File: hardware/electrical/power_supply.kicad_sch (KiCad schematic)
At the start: 0 parts

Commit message: initial commit of power module schematic and PCB
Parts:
- added C1: 4.7uF, Capacitor_SMD:C_0402_1005Metric, symbol Device:C
- added C2: 0.1uF, Capacitor_SMD:C_0402_1005Metric, symbol Device:C
- added C3: 10uF, Capacitor_SMD:C_0402_1005Metric, symbol Device:C
- added C4, C5: 1uF, Capacitor_SMD:C_0402_1005Metric, symbol Device:C
- added D1: LED, LED_SMD:LED_1206_3216Metric, symbol Device:LED
- added D2: D_Schottky, Diode_THT:D_DO-41_SOD81_P2.54mm_Vertical_AnodeUp, symbol Device:D_Schottky
- added J1: USB_OTG, Connector_USB:USB_Micro-B_GCT_USB3076-30-A, symbol Connector:USB_OTG
- added J2: Conn_01x02_Female, Connector_PinSocket_2.00mm:PinSocket_1x02_P2.00mm_Vertical, symbol Connector:Conn_01x02_Female
- added J3: Conn_01x02_Male, Connector_PinHeader_2.00mm:PinHeader_1x02_P2.00mm_Vertical, symbol Connector:Conn_01x02_Male
- added Q1, Q2: IRLZ34N, Package_TO_SOT_SMD:SOT-23, symbol Transistor_FET:IRLZ34N
- added Q3, Q4: IRLML5203, Package_TO_SOT_SMD:SOT-23, symbol Transistor_FET:IRLML5203
- added R1: R, Resistor_SMD:R_0805_2012Metric_Pad1.20x1.40mm_HandSolder, symbol Device:R
- added R2: 470, Resistor_SMD:R_0805_2012Metric_Pad1.20x1.40mm_HandSolder, symbol Device:R
- added R3: 2.7k, Resistor_SMD:R_0805_2012Metric_Pad1.20x1.40mm_HandSolder, symbol Device:R
- added R4: 100, Resistor_SMD:R_0805_2012Metric_Pad1.20x1.40mm_HandSolder, symbol Device:R
- added R5, R6: 1k, Resistor_SMD:R_0805_2012Metric_Pad1.20x1.40mm_HandSolder, symbol Device:R
- added SW1: SW_DIP_x01, Connector_PinHeader_2.00mm:PinHeader_1x02_P2.00mm_Vertical, symbol Switch:SW_DIP_x01
- added U1: MCP73831-2-OT, Package_TO_SOT_SMD:SOT-23-5, symbol Battery_Management:MCP73831-2-OT
- added U2: AP9101CK6, Package_TO_SOT_SMD:SOT-23-6, symbol Battery_Management:AP9101CK6
- added U3: MCP1700-3302E_SOT23, Package_TO_SOT_SMD:SOT-23, symbol Regulator_Linear:MCP1700-3302E_SOT23
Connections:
- new net: Q2.1 (G), U2.1 (DO)
- new net: Q1.2 (D), Q2.2 (D)
- new net: Q3.1 (G), Q4.1 (G), R6.1
- new net: C3.2, D2.1 (K), Q4.3 (D), SW1.1
- new net: Q3.2 (S), Q4.2 (S)
- new net: R1.2, U1.5 (PROG)
- new net: Q1.1 (G), U2.3 (CO)
- new net: R2.2, U1.1 (STAT)
- new net: R3.1, U2.2 (VM)
- new net: C2.2, R4.1, U2.5 (VDD)
- new net: D1.1 (K), R2.1
- new net +3V3: C5.2, J2.1 (Pin_1), U3.2 (VO)
- new net +5V: D1.2 (A), D2.2 (A), J1.1 (VBUS), R5.2, R6.2, U1.4 (VDD)
- new net GND: C1.1, C3.1, C4.1, C5.1, J1.5 (GND), J2.2 (Pin_2), Q1.3 (S), R1.1, R3.2, U1.2 (VSS), U3.1 (GND)
- new net LIPO+: C1.2, J3.1 (Pin_1), Q3.3 (D), R4.2, U1.3 (VBAT)
- new net LIPO-: C2.1, J3.2 (Pin_2), Q2.3 (S), R5.1, U2.6 (VSS)
- new net OUT+: C4.2, SW1.2, U3.3 (VI)
- no-connect marks 0 -> 4
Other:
- note added: "Battery Protection Circuit"
- note added: "Charge indicator"
- note added: "To LiPo"
- note added: "To Micro USB Charger"
- note added: "To Voltage Regulator"
- note added: "Voltage Regulators (LDO)"

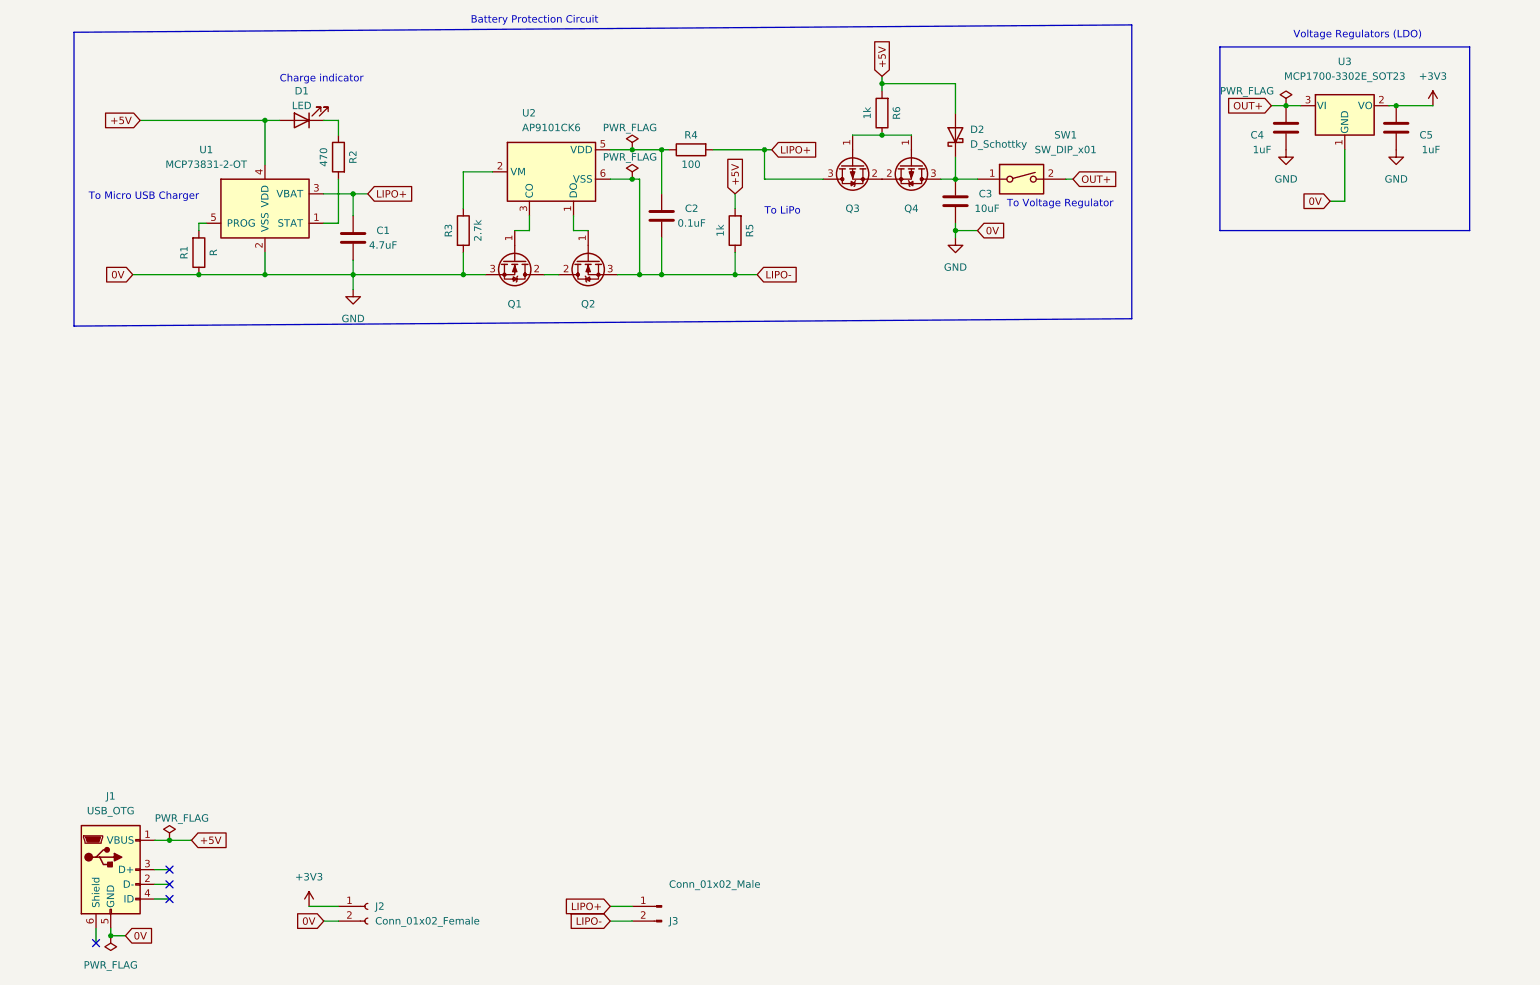
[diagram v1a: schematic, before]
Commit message: Power schematic style changes * Use power ports over global labels where possible * Replace 3.3V connector with test points * Make all component labels upright
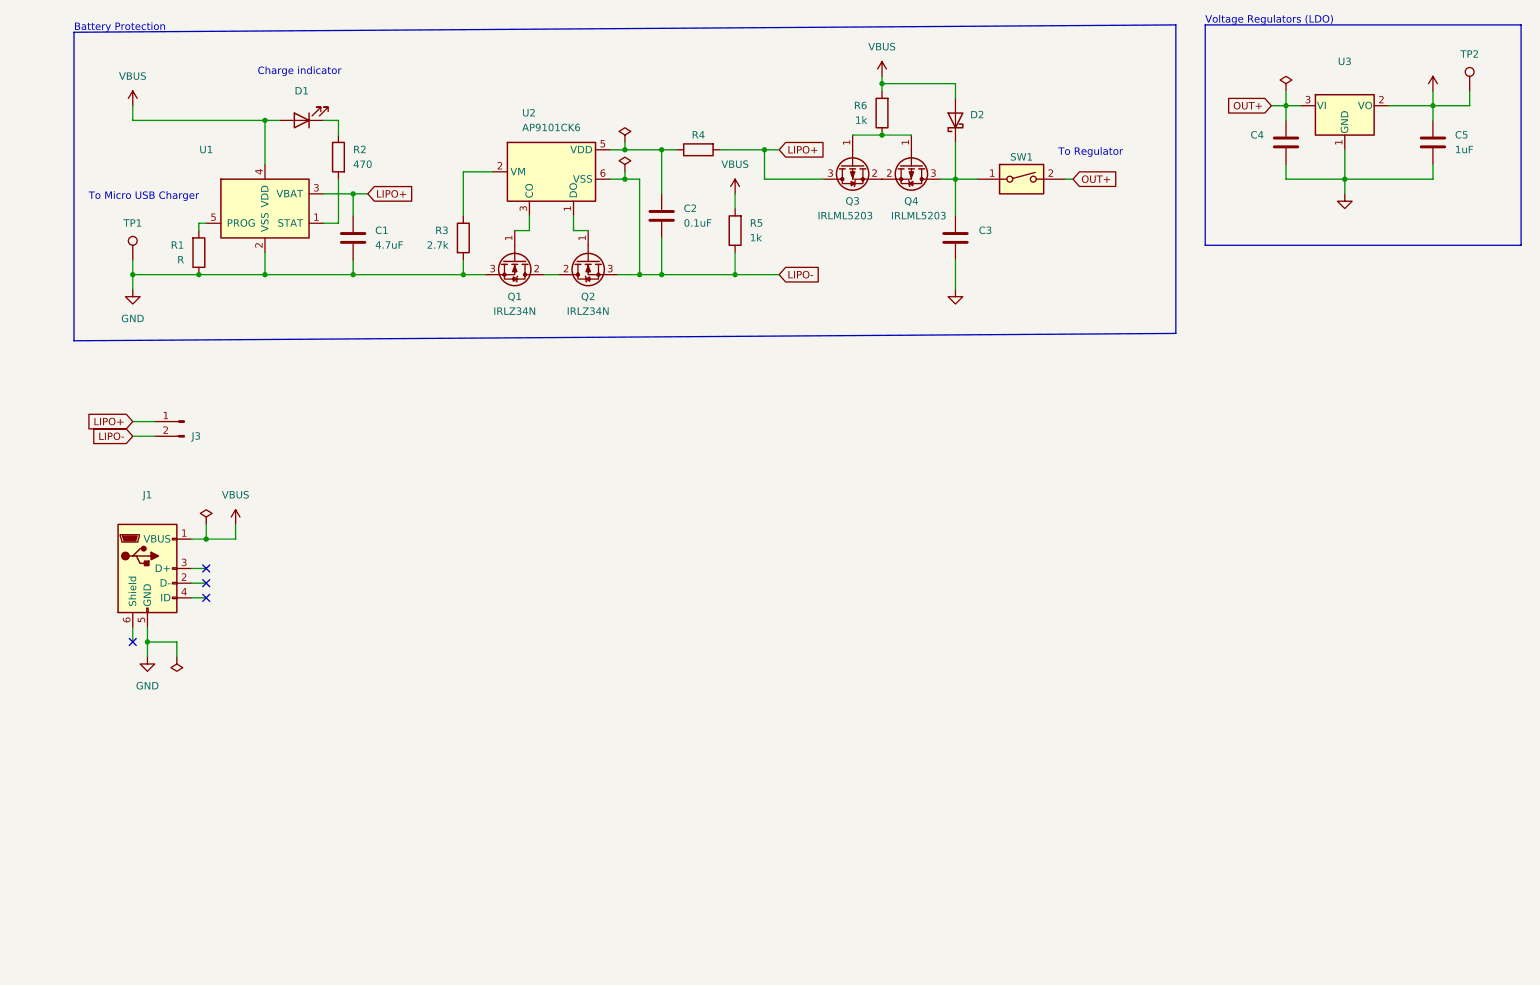
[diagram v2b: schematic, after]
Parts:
- removed J2: Conn_01x02_Female, Connector_PinSocket_2.00mm:PinSocket_1x02_P2.00mm_Vertical, symbol Connector:Conn_01x02_Female
- added TP1, TP2: TestPoint, symbol Connector:TestPoint
- C1, C2, C5: footprint Capacitor_SMD:C_0402_1005Metric -> (none)
- C3: value 10uF -> (none); footprint Capacitor_SMD:C_0402_1005Metric -> (none)
- C4: value 1uF -> (none); footprint Capacitor_SMD:C_0402_1005Metric -> (none)
- D1: value LED -> (none); footprint LED_SMD:LED_1206_3216Metric -> (none)
- D2: value D_Schottky -> (none); footprint Diode_THT:D_DO-41_SOD81_P2.54mm_Vertical_AnodeUp -> (none)
- J1: value USB_OTG -> (none); footprint Connector_USB:USB_Micro-B_GCT_USB3076-30-A -> (none)
- J3: value Conn_01x02_Male -> (none); footprint Connector_PinHeader_2.00mm:PinHeader_1x02_P2.00mm_Vertical -> (none)
- Q1, Q2, Q3, Q4: footprint Package_TO_SOT_SMD:SOT-23 -> (none)
- R1, R2, R3, R5, R6: footprint Resistor_SMD:R_0805_2012Metric_Pad1.20x1.40mm_HandSolder -> (none)
- R4: value 100 -> (none); footprint Resistor_SMD:R_0805_2012Metric_Pad1.20x1.40mm_HandSolder -> (none)
- SW1: value SW_DIP_x01 -> (none); footprint Connector_PinHeader_2.00mm:PinHeader_1x02_P2.00mm_Vertical -> (none)
- U1: value MCP73831-2-OT -> (none); footprint Package_TO_SOT_SMD:SOT-23-5 -> (none)
- U3: value MCP1700-3302E_SOT23 -> (none); footprint Package_TO_SOT_SMD:SOT-23 -> (none)
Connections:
- net +3V3: now also TP2.1
- net GND: now also TP1.1
- net +5V renamed VBUS
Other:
- note added: "Battery Protection"
- note added: "To Regulator"
- note removed: "Battery Protection Circuit"
- note removed: "To LiPo"
- note removed: "To Voltage Regulator"
- moved on the sheet: C3, C4, C5, D2, J1, J3, R3, R4

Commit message: grouped test points
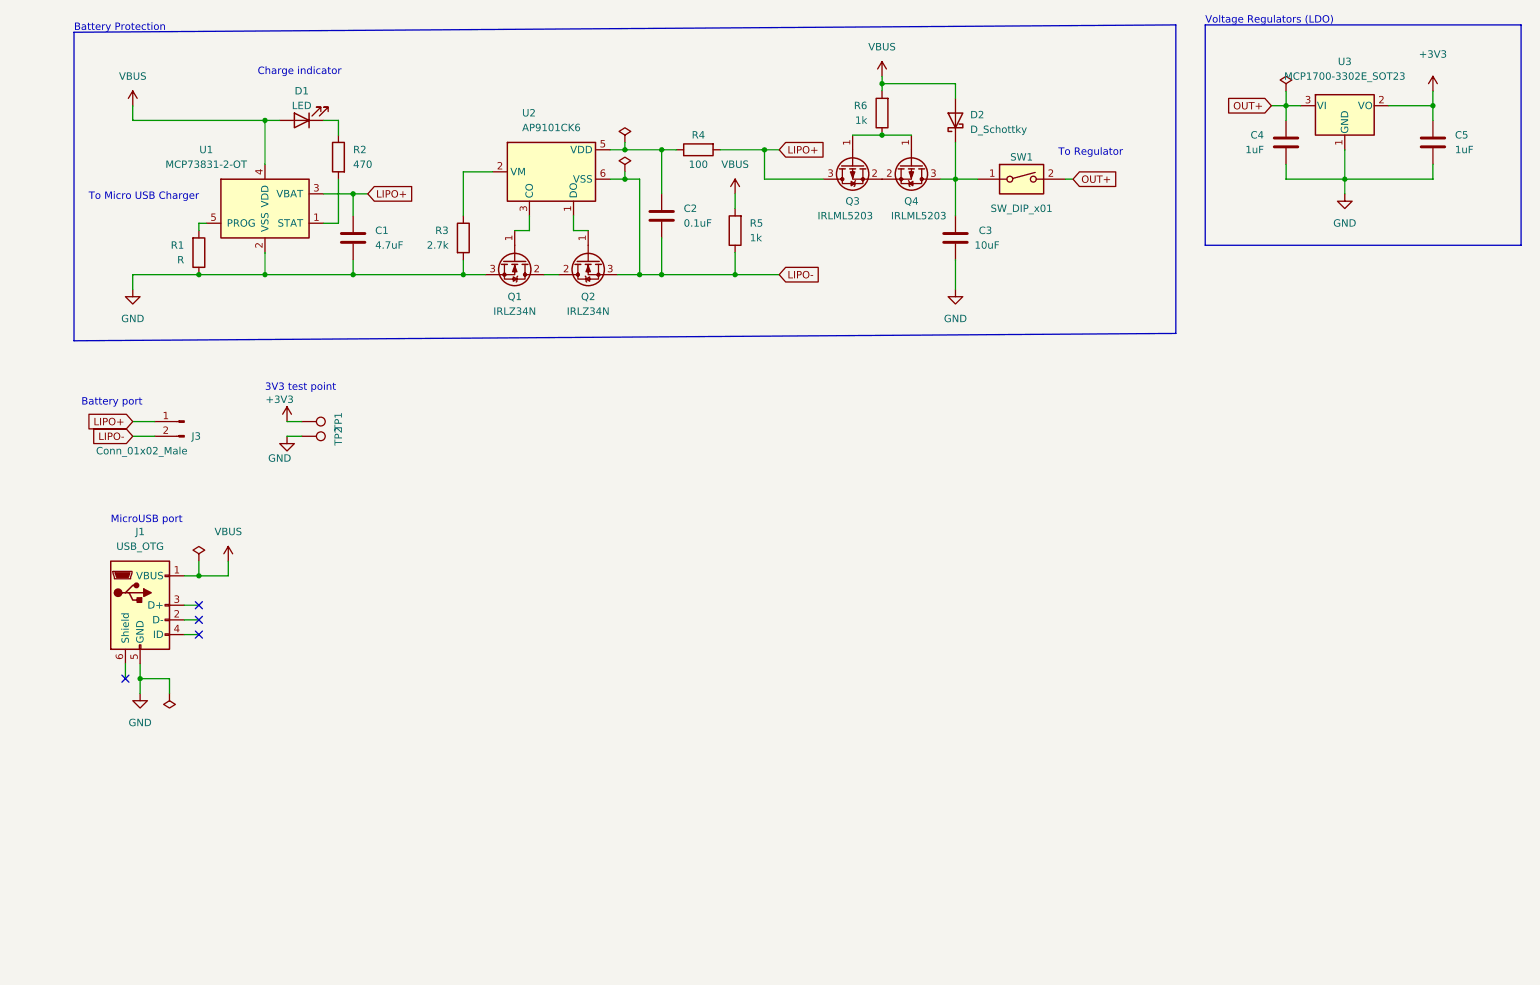
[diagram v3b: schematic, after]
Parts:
- C1, C2, C5: footprint (none) -> Capacitor_SMD:C_0402_1005Metric
- C3: value (none) -> 10uF; footprint (none) -> Capacitor_SMD:C_0402_1005Metric
- C4: value (none) -> 1uF; footprint (none) -> Capacitor_SMD:C_0402_1005Metric
- D1: value (none) -> LED; footprint (none) -> LED_SMD:LED_1206_3216Metric
- D2: value (none) -> D_Schottky; footprint (none) -> Diode_THT:D_DO-41_SOD81_P2.54mm_Vertical_AnodeUp
- J1: value (none) -> USB_OTG; footprint (none) -> Connector_USB:USB_Micro-B_GCT_USB3076-30-A
- J3: value (none) -> Conn_01x02_Male; footprint (none) -> Connector_PinHeader_2.00mm:PinHeader_1x02_P2.00mm_Vertical
- Q1, Q2, Q3, Q4: footprint (none) -> Package_TO_SOT_SMD:SOT-23
- R1, R2, R3, R5, R6: footprint (none) -> Resistor_SMD:R_0805_2012Metric_Pad1.20x1.40mm_HandSolder
- R4: value (none) -> 100; footprint (none) -> Resistor_SMD:R_0805_2012Metric_Pad1.20x1.40mm_HandSolder
- SW1: value (none) -> SW_DIP_x01; footprint (none) -> Connector_PinHeader_2.00mm:PinHeader_1x02_P2.00mm_Vertical
- U1: value (none) -> MCP73831-2-OT; footprint (none) -> Package_TO_SOT_SMD:SOT-23-5
- U3: value (none) -> MCP1700-3302E_SOT23; footprint (none) -> Package_TO_SOT_SMD:SOT-23
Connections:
- net +3V3: now also TP1.1; no longer TP2.1
- net GND: now also TP2.1; no longer TP1.1
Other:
- note added: "3V3 test point"
- note added: "Battery port"
- note added: "MicroUSB port"
- moved on the sheet: J1, TP1, TP2
